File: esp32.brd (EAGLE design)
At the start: 91.4 x 79.7 mm, 65 parts, among them IC1 PEC11R-4230K-S00243D, IC2 AD8532ARZ, T1 BST82-1, T2 BST82-1, T3 BST82-1, U1 ESP32-WROOM-32D, X1 JST-XH-02-PIN-LONG-PAD, X2 JST-XH-03-PIN-LONG-PAD, X3 JST-XH-03-PIN-LONG-PAD, X4 JST-XH-02-PIN-LONG-PAD

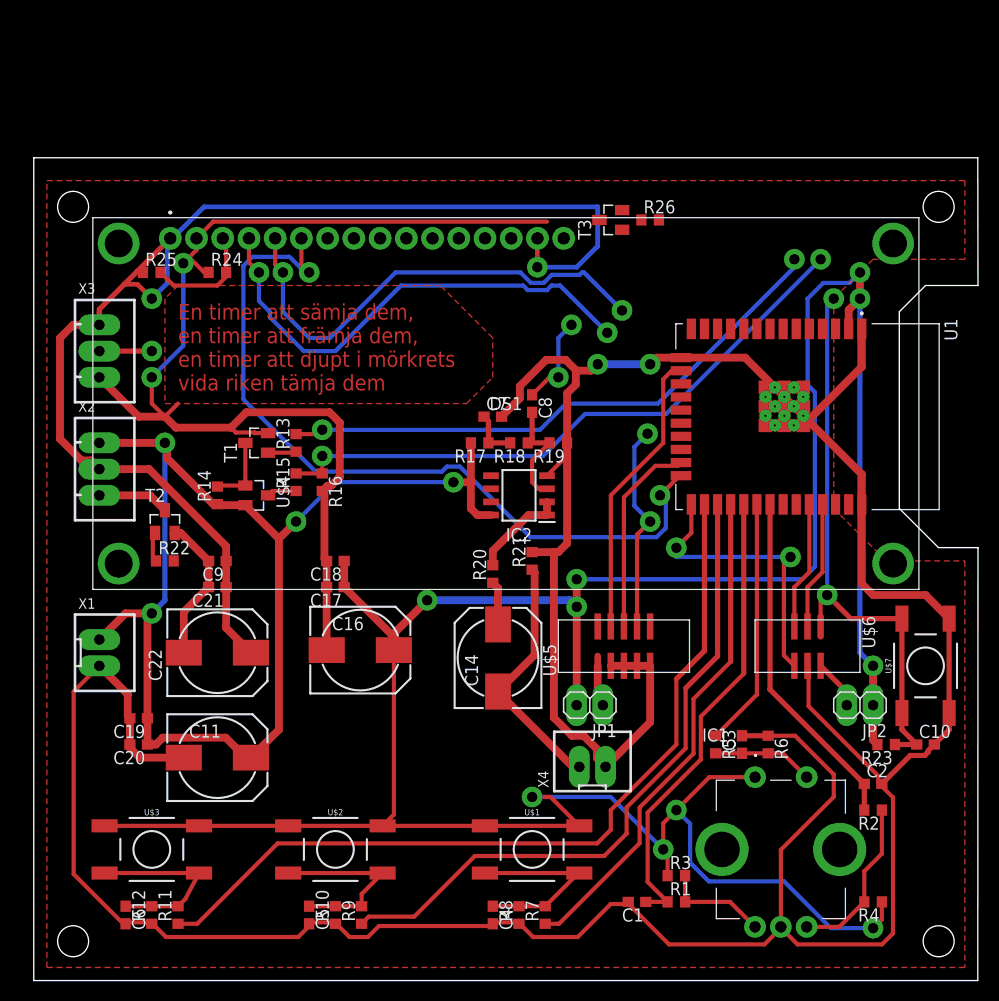
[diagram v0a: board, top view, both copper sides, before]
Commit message: Alla diken är nu 18mil. Nästa är att koppla de sista signalerna till esp32
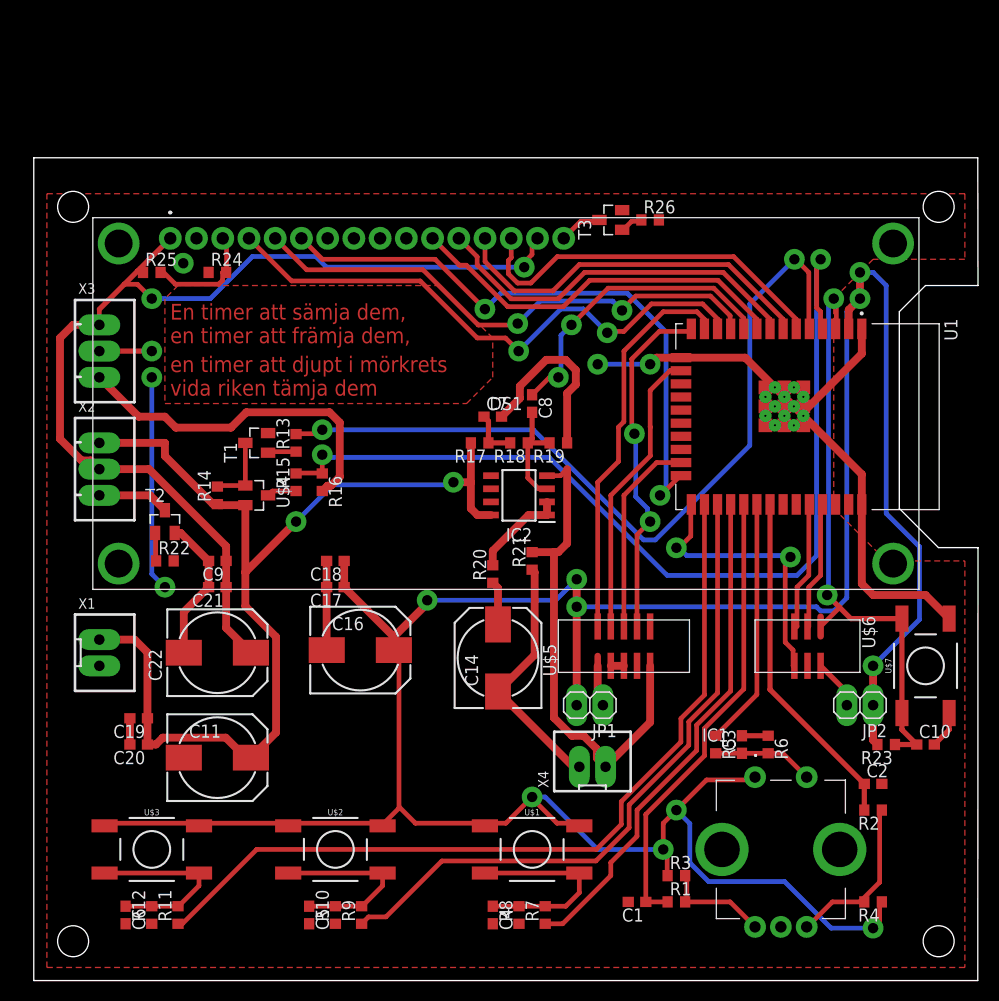
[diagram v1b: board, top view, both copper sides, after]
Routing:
- net GND: track 489.4 -> 216.5 mm, vias 4 -> 5
- net TMS: track 0.00 -> 38.3 mm
- net LCD_D4: track 0.00 -> 37.7 mm
- net LCD_D5: track 0.00 -> 36.9 mm
- net LCD_D6: track 0.00 -> 36.5 mm
- net LCD_D7: track 0.00 -> 36.3 mm
- net BAT_MONITOR_ANALOG: track 60.4 -> 93.9 mm
- net BAT_MONITOR_ENABLE: track 55.7 -> 79.5 mm
- net +5V: track 125.8 -> 102.4 mm
- net AUDIO_FROM_ESP32: track 8.85 -> 29.2 mm
- net VCC: track 121.7 -> 103.3 mm, vias 4 -> 2
- net LCD_E: track 77.3 -> 59.2 mm
- net TDI: track 20.4 -> 34.4 mm
- net LCD_RS: track 47.4 -> 55.3 mm
- net LCD_RW: track 46.3 -> 51.6 mm
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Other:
- board text added: "En timer att sämja dem, en timer att främja dem,"
- board text added: "en timer att djupt i mörkrets vida riken tämja dem"
- board text removed: "En timer att sämja dem, en timer att främja dem, en timer att djupt i mörkrets vida riken tämja dem"

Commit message: Kopplade alla signaler, ska göra om footprint för LCD och sen sätta på 3.3V regulator och sen borde den vara komplett!
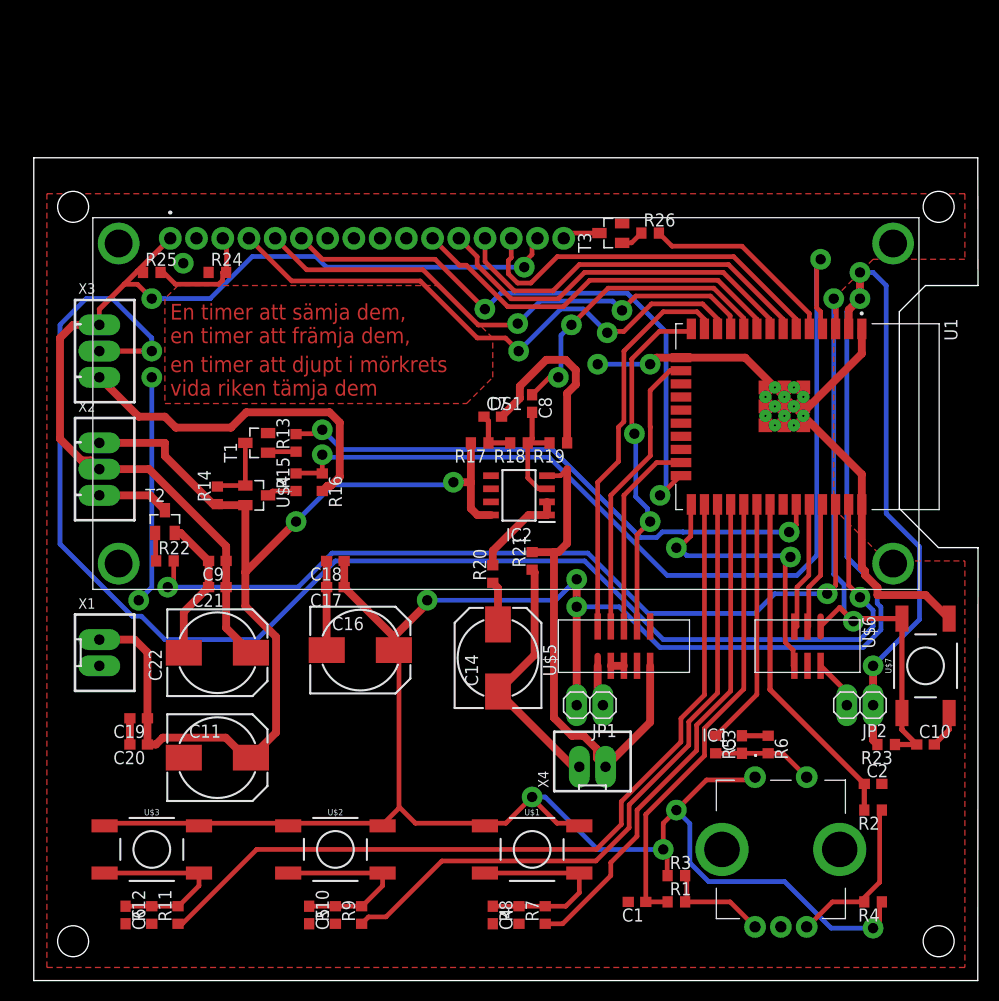
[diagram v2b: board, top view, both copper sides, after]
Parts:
- moved R26 1.27 mm to (59.7, 72.4)
- moved T3 1.27 mm to (55.9, 72.4)
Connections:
- net BAT_MONITOR_ENABLE: now also U1.33; no longer U1.5
- net ENABLE_5V: now also U1.36
- net LCD_DIMMER: now also U1.5
- net WS2812B_DATA: now also U1.37
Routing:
- net WS2812B_DATA: track 5.08 -> 141.3 mm, vias 1 -> 2
- net ENABLE_5V: track 0.00 -> 80.2 mm, vias 0 -> 2
- net BAT_MONITOR_ENABLE: track 79.5 -> 55.4 mm
- net LCD_DIMMER: track 0.00 -> 19.3 mm
- net +3V3: track 282.4 -> 291.8 mm
- net ESP_EN: track 58.2 -> 59.8 mm
- net GND: track 216.5 -> 217.5 mm
- net N$18: track 4.18 -> 3.67 mm

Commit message: Delade upp i lite olika plan. Rätta footprints för kondingar och 3.3V regulator.
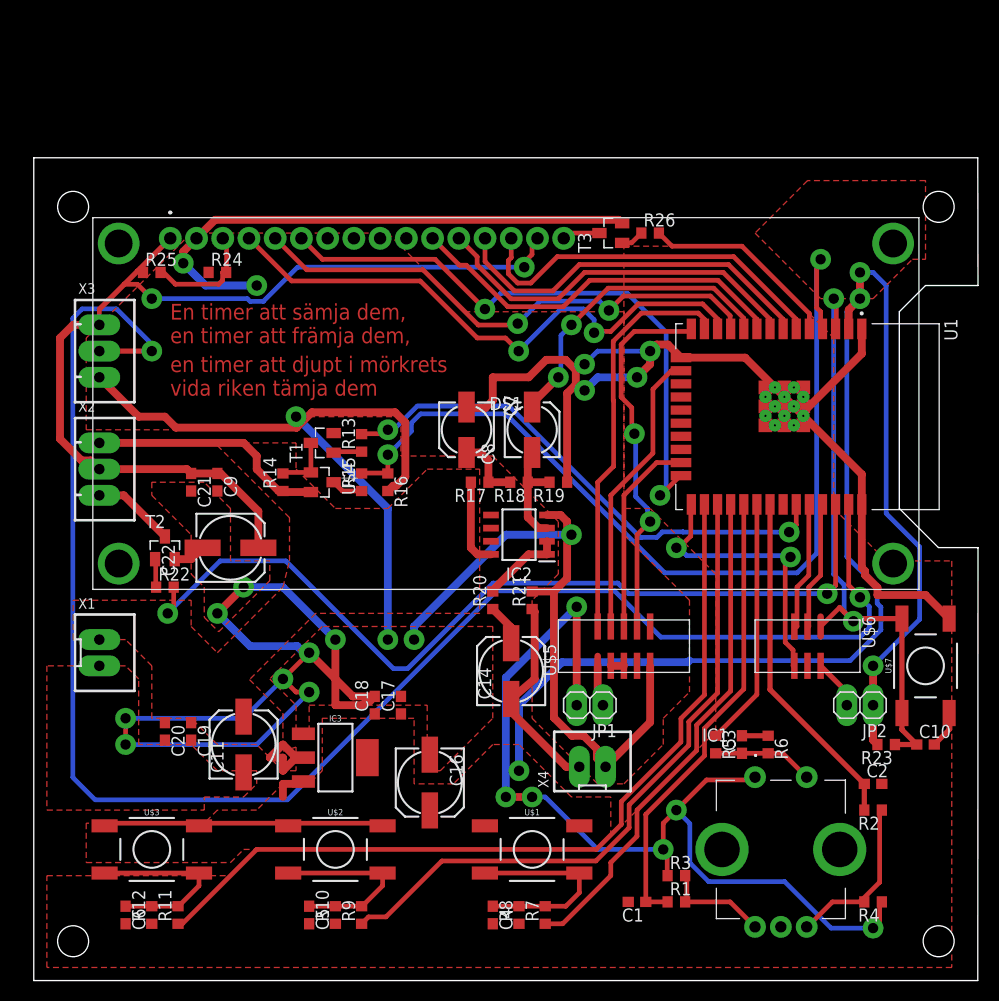
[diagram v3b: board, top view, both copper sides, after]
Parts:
- added IC3: LM1117MP-3.3_NOPBSMD, Test:SOT223
- C11, C14, C22: device rcl:140CLH-0810 -> rcl:153CLV-0605
- C16: value (none) -> 100uF; device rcl:140CLH-0810 -> rcl:153CLV-0605
- C7, C8: device rcl:C0603 -> rcl:153CLV-0505
- moved C16 14.5 mm to (38.4, 19.2), turned to 270 degrees
- moved C18 14.5 mm to (33.0, 26.7), turned to 90 degrees
- moved C17 13.1 mm to (35.6, 26.7), turned to 90 degrees
- moved C21 10.5 mm to (15.2, 48.3), turned to 270 degrees
- moved C22 10.2 mm to (19.1, 41.9)
- moved C9 7.62 mm to (17.8, 48.3), turned to 270 degrees
- moved U$4 6.48 mm to (27.9, 48.3)
- moved R14 6.48 mm to (24.1, 48.3)
- moved R13 6.35 mm to (31.8, 52.1)
- moved R15 6.35 mm to (31.8, 48.3)
- moved T1 6.35 mm to (27.9, 52.1)
- moved R16 6.35 mm to (34.3, 48.3)
- moved C19 5.24 mm to (15.2, 24.1), turned to 270 degrees
- moved IC2 3.81 mm to (47.0, 43.2)
- moved R17 3.81 mm to (43.2, 48.3)
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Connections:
- net +3V3: now also IC3.3, IC3.4
- net AUDIO_FROM_ESP32: now also C8.+; no longer C8.1
- net GND: now also C7.-, IC3.1; no longer C7.2
- net N$10: now also C7.+; no longer C7.1
- net N$4: now also C8.-; no longer C8.2
- net VCC: now also IC3.2
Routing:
- net GND: track 217.5 -> 381.7 mm, vias 5 -> 18
- net VCC: track 103.3 -> 40.4 mm, vias 2 -> 0
- net +3V3: track 291.8 -> 259.5 mm
- net WS2812B_DATA: track 141.3 -> 161.1 mm
- net +5V: track 102.4 -> 95.7 mm
- net ENABLE_5V: track 80.2 -> 85.9 mm
- net BAT_MONITOR_ENABLE: track 55.4 -> 51.0 mm
- net SPEAKER_OUT: track 24.3 -> 19.9 mm
- net BAT_MONITOR_ANALOG: track 93.9 -> 90.9 mm
- net TDI: track 34.4 -> 36.6 mm
- net N$10: track 4.83 -> 6.66 mm
- net N$7: track 6.88 -> 5.61 mm
- net N$12: track 9.36 -> 8.09 mm
- net TMS: track 38.3 -> 39.4 mm
- net N$15: track 6.95 -> 8.00 mm
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- added copper zone on layer 1, net +3V3
- added copper zone on layer 1, net VCC

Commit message: En lite fix till. :)
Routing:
- net WS2812B_DATA: track 161.1 -> 154.3 mm
- net +3V3: track 259.5 -> 255.3 mm
- net BAT_MONITOR_ANALOG: track 90.9 -> 87.2 mm
- net BAT_MONITOR_ENABLE: track 51.0 -> 49.1 mm
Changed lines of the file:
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@@
 <wire x1="77.22058125" y1="5.08" x2="72.71448125" y2="9.5861" width="0.4572" layer="16"/>
 <wire x1="72.71448125" y1="9.5861" x2="65.360175" y2="9.5861" width="0.4572" layer="16"/>
-<wire x1="78.74" y1="64.77" x2="80.01" y2="66.04" width="0.4572" layer="16"/>
 <wire x1="81.28" y1="30.48" x2="85.7784" y2="34.9784" width="0.4572" layer="16"/>
 <wire x1="85.7784" y1="34.9784" x2="85.7784" y2="42.00146875" width="0.4572" layer="16"/>
@@
 <wire x1="81.28" y1="68.58" x2="80.01" y2="68.58" width="0.4572" layer="16"/>
 <wire x1="85.7784" y1="42.00146875" x2="82.55" y2="45.22986875" width="0.4572" layer="16"/>
-<wire x1="81.6784" y1="38.103475" x2="78.74" y2="41.041875" width="0.4572" layer="16"/>
-<wire x1="78.74" y1="41.041875" x2="78.74" y2="64.77" width="0.4572" layer="16"/>
-<wire x1="82.042" y1="33.97436875" x2="82.042" y2="36.16443125" width="0.4572" layer="16"/>
-<wire x1="82.042" y1="36.16443125" x2="81.6784" y2="36.52803125" width="0.4572" layer="16"/>
-<wire x1="81.6784" y1="36.52803125" x2="81.6784" y2="38.103475" width="0.4572" layer="16"/>
-<wire x1="79.05563125" y1="30.988" x2="82.042" y2="33.97436875" width="0.4572" layer="16"/>
 <contactref element="IC3" pad="3"/>
 <contactref element="IC3" pad="4"/>
@@
 <via x="46.99" y="20.32" extent="1-16" drill="1"/>
 <wire x1="45.72" y1="29.337" x2="52.578" y2="36.195" width="0.762" layer="16"/>
-<wire x1="46.99" y1="20.32" x2="46.99" y2="26.67" width="0.762" layer="16"/>
-<wire x1="51.1556" y1="30.8356" x2="46.99" y2="26.67" width="0.762" layer="16"/>
-<wire x1="63.5" y1="30.988" x2="63.3476" y2="30.8356" width="0.762" layer="16"/>
-<wire x1="63.3476" y1="30.8356" x2="51.1556" y2="30.8356" width="0.762" layer="16"/>
-<wire x1="63.5" y1="30.988" x2="79.05563125" y2="30.988" width="0.4572" layer="16"/>
 <polygon width="0.4572" layer="1">
 <vertex x="76.2" y="66.04"/>
@@
 <vertex x="69.85" y="72.39"/>
 </polygon>
+<wire x1="46.99" y1="20.32" x2="46.99" y2="21.9647125" width="0.762" layer="16"/>
+<wire x1="63.5" y1="30.988" x2="78.82250625" y2="30.988" width="0.4572" layer="16"/>
+<wire x1="78.82250625" y1="30.988" x2="81.6784" y2="33.84389375" width="0.4572" layer="16"/>
+<wire x1="81.6784" y1="38.103475" x2="80.01" y2="39.771875" width="0.4572" layer="16"/>
+<wire x1="80.01" y1="39.771875" x2="80.01" y2="66.04" width="0.4572" layer="16"/>
+<wire x1="81.6784" y1="33.84389375" x2="81.6784" y2="38.103475" width="0.4572" layer="16"/>
+<wire x1="56.0132875" y1="30.988" x2="63.5" y2="30.988" width="0.762" layer="16"/>
+<wire x1="46.99" y1="21.9647125" x2="56.0132875" y2="30.988" width="0.762" layer="16"/>
 </signal>
 <signal name="N$3">
@@
 <wire x1="60.871275" y1="43.4514" x2="60.328475" y2="42.9086" width="0.4572" layer="16"/>
 <wire x1="60.328475" y1="42.9086" x2="58.75303125" y2="42.9086" width="0.4572" layer="16"/>
-<wire x1="34.84249375" y1="53.34" x2="34.29" y2="53.34" width="0.4572" layer="16"/>
-<wire x1="37.14589375" y1="55.6434" x2="34.84249375" y2="53.34" width="0.4572" layer="16"/>
-<wire x1="58.75303125" y1="42.9086" x2="46.01823125" y2="55.6434" width="0.4572" layer="16"/>
-<wire x1="46.01823125" y1="55.6434" x2="37.14589375" y2="55.6434" width="0.4572" layer="16"/>
+<wire x1="58.75303125" y1="42.9086" x2="48.32163125" y2="53.34" width="0.4572" layer="16"/>
+<wire x1="48.32163125" y1="53.34" x2="34.29" y2="53.34" width="0.4572" layer="16"/>
 </signal>
 <signal name="VCC">
@@
 <wire x1="76.2" y1="69.723" x2="75.819" y2="69.342" width="0.4572" layer="16"/>
 <wire x1="76.2" y1="69.85" x2="76.2" y2="69.723" width="0.4572" layer="16"/>
-<wire x1="37.461525" y1="54.8814" x2="36.5586" y2="53.978475" width="0.4572" layer="16"/>
 <wire x1="75.819" y1="69.342" x2="75.819" y2="41.381125" width="0.4572" layer="16"/>
 <wire x1="75.819" y1="41.381125" x2="73.917475" y2="39.4796" width="0.4572" layer="16"/>
 <wire x1="73.917475" y1="39.4796" x2="61.1044" y2="39.4796" width="0.4572" layer="16"/>
-<wire x1="61.1044" y1="39.4796" x2="45.7026" y2="54.8814" width="0.4572" layer="16"/>
-<wire x1="45.7026" y1="54.8814" x2="37.461525" y2="54.8814" width="0.4572" layer="16"/>
-<wire x1="36.5586" y1="53.978475" x2="36.5586" y2="53.1956" width="0.4572" layer="16"/>
-<wire x1="36.5586" y1="53.1956" x2="34.29" y2="50.927" width="0.4572" layer="16"/>
+<wire x1="61.1044" y1="39.4796" x2="49.657" y2="50.927" width="0.4572" layer="16"/>
+<wire x1="49.657" y1="50.927" x2="34.29" y2="50.927" width="0.4572" layer="16"/>
 </signal>
 <signal name="N$13">
@@
 <wire x1="73.533" y1="30.48" x2="73.66" y2="30.48" width="0.4572" layer="1"/>
 <wire x1="73.152" y1="40.767" x2="73.279" y2="41.021" width="0.4572" layer="1"/>
-<wire x1="63.246" y1="41.148" x2="73.152" y2="41.148" width="0.4572" layer="16"/>
-<wire x1="62.484" y1="41.91" x2="63.246" y2="41.148" width="0.4572" layer="16"/>
-<wire x1="73.152" y1="41.148" x2="73.279" y2="41.021" width="0.4572" layer="16"/>
-<wire x1="62.484" y1="41.91" x2="62.23" y2="41.91" width="0.4572" layer="16"/>
+<wire x1="62.23" y1="41.91" x2="72.39" y2="41.91" width="0.4572" layer="16"/>
+<wire x1="72.39" y1="41.91" x2="73.279" y2="41.021" width="0.4572" layer="16"/>
 </signal>
 <signal name="LCD_D7">
@@
 <wire x1="60.7234" y1="33.2566" x2="56.2436" y2="37.7364" width="0.4572" layer="16"/>
 <wire x1="56.2436" y1="37.7364" x2="44.80390625" y2="37.7364" width="0.4572" layer="16"/>
-<wire x1="5.9622125" y1="17.5006" x2="3.7846" y2="19.6782125" width="0.4572" layer="16"/>
-<wire x1="3.7846" y1="19.6782125" x2="3.7846" y2="64.1417875" width="0.4572" layer="16"/>
 <wire x1="3.7846" y1="64.1417875" x2="4.6922125" y2="65.0494" width="0.4572" layer="16"/>
 <wire x1="4.6922125" y1="65.0494" x2="8.0077875" y2="65.0494" width="0.4572" layer="16"/>
 <wire x1="8.0077875" y1="65.0494" x2="11.43" y2="61.6271875" width="0.4572" layer="16"/>
 <wire x1="11.43" y1="61.6271875" x2="11.43" y2="60.96" width="0.4572" layer="16"/>
-<wire x1="44.80390625" y1="37.7364" x2="24.56810625" y2="17.5006" width="0.4572" layer="16"/>
-<wire x1="24.56810625" y1="17.5006" x2="5.9622125" y2="17.5006" width="0.4572" layer="16"/>
+<wire x1="44.80390625" y1="37.7364" x2="28.38610625" y2="21.3186" width="0.4572" layer="16"/>
+<wire x1="28.38610625" y1="21.3186" x2="8.251525" y2="21.3186" width="0.4572" layer="16"/>
+<wire x1="8.251525" y1="21.3186" x2="3.7846" y2="25.785525" width="0.4572" layer="16"/>
+<wire x1="3.7846" y1="25.785525" x2="3.7846" y2="64.1417875" width="0.4572" layer="16"/>
 </signal>
 <signal name="N$17">
